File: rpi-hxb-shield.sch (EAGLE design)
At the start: 30 parts, among them Q1 CRYSTALX22, U2 24LC128-I/SN

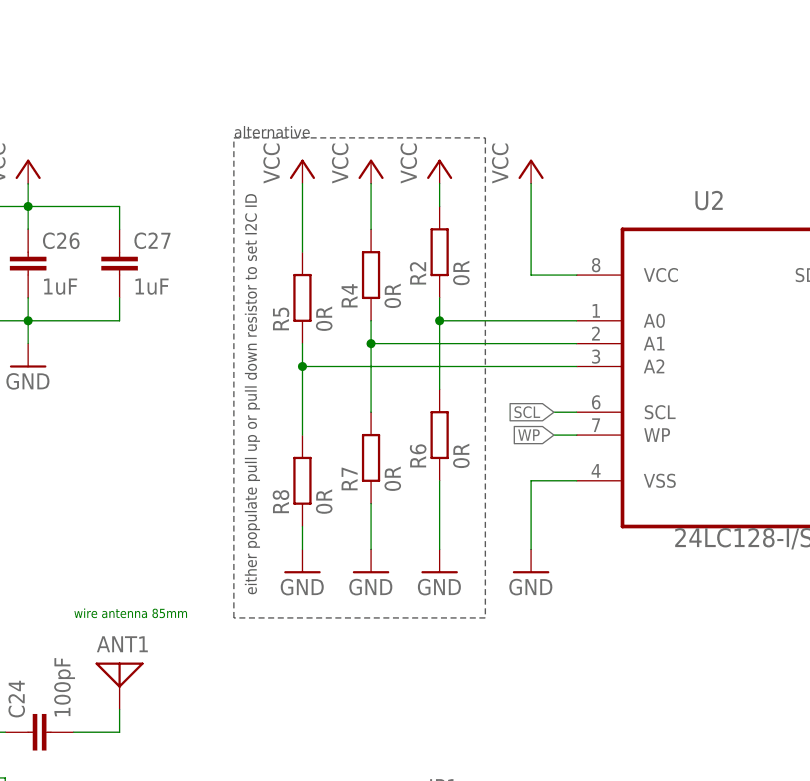
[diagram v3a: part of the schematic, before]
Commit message: EEPOM now with fixed address (hardwired)
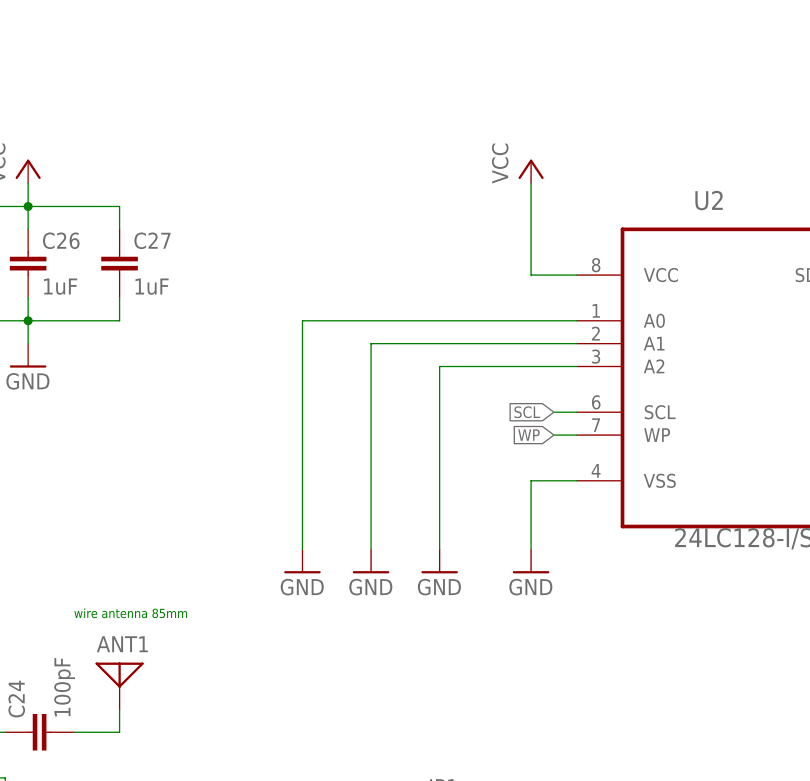
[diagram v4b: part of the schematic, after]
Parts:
- removed R2, R4, R5, R6, R7, R8: 0R, rcl:R-EU_R0603
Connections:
- removed net N$10: R5.1, R8.2, U2.A2
- removed net N$4: R2.1, R6.2, U2.A0
- removed net N$9: R4.1, R7.2, U2.A1
- net GND: now also U2.A0, U2.A1, U2.A2; no longer R6.1, R7.1, R8.1
- net VCC: no longer R2.2, R4.2, R5.2
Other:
- note removed: "alternative"
- note removed: "either populate pull up or pull down resistor to set I2C ID"
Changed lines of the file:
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@@
 <part name="P+1" library="supply1" deviceset="VCC" device=""/>
 <part name="GND8" library="supply1" deviceset="GND" device=""/>
-<part name="R2" library="rcl" deviceset="R-EU_" device="R0603" value="0R"/>
-<part name="R4" library="rcl" deviceset="R-EU_" device="R0603" value="0R"/>
-<part name="R5" library="rcl" deviceset="R-EU_" device="R0603" value="0R"/>
-<part name="P+2" library="supply1" deviceset="VCC" device=""/>
-<part name="P+3" library="supply1" deviceset="VCC" device=""/>
-<part name="P+6" library="supply1" deviceset="VCC" device=""/>
-<part name="R6" library="rcl" deviceset="R-EU_" device="R0603" value="0R"/>
-<part name="R7" library="rcl" deviceset="R-EU_" device="R0603" value="0R"/>
-<part name="R8" library="rcl" deviceset="R-EU_" device="R0603" value="0R"/>
 <part name="GND9" library="supply1" deviceset="GND" device=""/>
 <part name="GND10" library="supply1" deviceset="GND" device=""/>
@@
 <text x="154.94" y="119.38" size="1.016" layer="91">wire antenna 85mm</text>
 <text x="119.38" y="43.18" size="1.016" layer="91">solder pads for antenna</text>
-<wire x1="172.72" y1="172.72" x2="200.66" y2="172.72" width="0.1524" layer="97" style="longdash"/>
-<wire x1="200.66" y1="172.72" x2="200.66" y2="119.38" width="0.1524" layer="97" style="longdash"/>
-<wire x1="200.66" y1="119.38" x2="172.72" y2="119.38" width="0.1524" layer="97" style="longdash"/>
-<wire x1="172.72" y1="119.38" x2="172.72" y2="172.72" width="0.1524" layer="97" style="longdash"/>
-<text x="172.72" y="172.72" size="1.27" layer="97">alternative</text>
-<text x="175.26" y="121.92" size="1.27" layer="97" rot="R90">either populate pull up or pull down resistor to set I2C ID</text>
 </plain>
 <instances>
@@
 <instance part="P+1" gate="VCC" x="205.74" y="170.18"/>
 <instance part="GND8" gate="1" x="205.74" y="124.46"/>
-<instance part="R2" gate="G$1" x="195.58" y="160.02" rot="R90"/>
-<instance part="R4" gate="G$1" x="187.96" y="157.48" rot="R90"/>
-<instance part="R5" gate="G$1" x="180.34" y="154.94" rot="R90"/>
-<instance part="P+2" gate="VCC" x="195.58" y="170.18"/>
-<instance part="P+3" gate="VCC" x="187.96" y="170.18"/>
-<instance part="P+6" gate="VCC" x="180.34" y="170.18"/>
-<instance part="R6" gate="G$1" x="195.58" y="139.7" rot="R90"/>
-<instance part="R7" gate="G$1" x="187.96" y="137.16" rot="R90"/>
-<instance part="R8" gate="G$1" x="180.34" y="134.62" rot="R90"/>
 <instance part="GND9" gate="1" x="195.58" y="124.46"/>
 <instance part="GND10" gate="1" x="187.96" y="124.46"/>
@@
 </segment>
 <segment>
-<pinref part="R8" gate="G$1" pin="1"/>
-<pinref part="GND11" gate="1" pin="GND"/>
-<wire x1="180.34" y1="129.54" x2="180.34" y2="127" width="0.1524" layer="91"/>
-</segment>
-<segment>
-<pinref part="R7" gate="G$1" pin="1"/>
-<pinref part="GND10" gate="1" pin="GND"/>
-<wire x1="187.96" y1="132.08" x2="187.96" y2="127" width="0.1524" layer="91"/>
-</segment>
-<segment>
-<pinref part="R6" gate="G$1" pin="1"/>
-<pinref part="GND9" gate="1" pin="GND"/>
-<wire x1="195.58" y1="134.62" x2="195.58" y2="127" width="0.1524" layer="91"/>
-</segment>
-<segment>
 <pinref part="JP1" gate="A" pin="25"/>
 <wire x1="198.12" y1="66.04" x2="190.5" y2="66.04" width="0.1524" layer="91"/>
@@
 <wire x1="205.74" y1="73.66" x2="213.36" y2="73.66" width="0.1524" layer="91"/>
 <label x="213.36" y="73.66" size="1.27" layer="95" xref="yes"/>
+</segment>
+<segment>
+<pinref part="GND9" gate="1" pin="GND"/>
+<pinref part="U2" gate="A" pin="A2"/>
+<wire x1="195.58" y1="127" x2="195.58" y2="147.32" width="0.1524" layer="91"/>
+<wire x1="195.58" y1="147.32" x2="210.82" y2="147.32" width="0.1524" layer="91"/>
+</segment>
+<segment>
+<pinref part="GND10" gate="1" pin="GND"/>
+<pinref part="U2" gate="A" pin="A1"/>
+<wire x1="187.96" y1="127" x2="187.96" y2="149.86" width="0.1524" layer="91"/>
+<wire x1="187.96" y1="149.86" x2="210.82" y2="149.86" width="0.1524" layer="91"/>
+</segment>
+<segment>
+<pinref part="GND11" gate="1" pin="GND"/>
+<pinref part="U2" gate="A" pin="A0"/>
+<wire x1="180.34" y1="127" x2="180.34" y2="152.4" width="0.1524" layer="91"/>
+<wire x1="180.34" y1="152.4" x2="210.82" y2="152.4" width="0.1524" layer="91"/>
 </segment>
 </net>
@@
 </segment>
 <segment>
-<pinref part="P+6" gate="VCC" pin="VCC"/>
-<pinref part="R5" gate="G$1" pin="2"/>
-<wire x1="180.34" y1="167.64" x2="180.34" y2="160.02" width="0.1524" layer="91"/>
-</segment>
-<segment>
-<pinref part="P+3" gate="VCC" pin="VCC"/>
-<pinref part="R4" gate="G$1" pin="2"/>
-<wire x1="187.96" y1="167.64" x2="187.96" y2="162.56" width="0.1524" layer="91"/>
-</segment>
-<segment>
-<pinref part="P+2" gate="VCC" pin="VCC"/>
-<pinref part="R2" gate="G$1" pin="2"/>
-<wire x1="195.58" y1="167.64" x2="195.58" y2="165.1" width="0.1524" layer="91"/>
-</segment>
-<segment>
 <pinref part="JP1" gate="A" pin="1"/>
 <wire x1="198.12" y1="96.52" x2="190.5" y2="96.52" width="0.1524" layer="91"/>
@@
 </segment>
 </net>
-<net name="N$4" class="0">
-<segment>
-<pinref part="U2" gate="A" pin="A0"/>
-<pinref part="R2" gate="G$1" pin="1"/>
-<wire x1="210.82" y1="152.4" x2="195.58" y2="152.4" width="0.1524" layer="91"/>
-<wire x1="195.58" y1="152.4" x2="195.58" y2="154.94" width="0.1524" layer="91"/>
-<pinref part="R6" gate="G$1" pin="2"/>
-<wire x1="195.58" y1="144.78" x2="195.58" y2="152.4" width="0.1524" layer="91"/>
-<junction x="195.58" y="152.4"/>
-</segment>
-</net>
-<net name="N$9" class="0">
-<segment>
-<pinref part="U2" gate="A" pin="A1"/>
-<pinref part="R4" gate="G$1" pin="1"/>
-<wire x1="210.82" y1="149.86" x2="187.96" y2="149.86" width="0.1524" layer="91"/>
-<wire x1="187.96" y1="149.86" x2="187.96" y2="152.4" width="0.1524" layer="91"/>
-<pinref part="R7" gate="G$1" pin="2"/>
-<wire x1="187.96" y1="142.24" x2="187.96" y2="149.86" width="0.1524" layer="91"/>
-<junction x="187.96" y="149.86"/>
-</segment>
-</net>
-<net name="N$10" class="0">
-<segment>
-<pinref part="U2" gate="A" pin="A2"/>
-<pinref part="R5" gate="G$1" pin="1"/>
-<wire x1="210.82" y1="147.32" x2="180.34" y2="147.32" width="0.1524" layer="91"/>
-<wire x1="180.34" y1="147.32" x2="180.34" y2="149.86" width="0.1524" layer="91"/>
-<pinref part="R8" gate="G$1" pin="2"/>
-<wire x1="180.34" y1="139.7" x2="180.34" y2="147.32" width="0.1524" layer="91"/>
-<junction x="180.34" y="147.32"/>
-</segment>
-</net>
